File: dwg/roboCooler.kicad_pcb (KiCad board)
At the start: 2 copper layers, 100 x 81 mm, 54 parts, among them J1 CONN_01X02, J10 CONN_01X04, J11 CONN_01X04, J12 USB_A, J13 CONN_02X03, J14 CONN_02X03, J2 CONN_01X02, J3 Discovery_F407_P1, J4 CONN_01X06, J5 CONN_01X12, J6 Discovery_F407_P2, J7 CONN_02X03, J8 CONN_01X02, J9 CONN_01X02, Q1 NMOS, Q2 NMOS, SW1 SPST_4PIN, SW2 SPST_4PIN, U1 SN74LV, U2 TB6549

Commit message: moved led fan and pump to 6-pin conns
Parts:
- removed J9: CONN_01X02, Socket_Strips:Socket_Strip_Angled_1x02
- J10: value CONN_01X04 -> CONN_02X03; footprint Socket_Strips:Socket_Strip_Angled_1x04 -> Pin_Headers:Pin_Header_Angled_2x03
- J8: value CONN_01X02 -> CONN_02X03; footprint Socket_Strips:Socket_Strip_Angled_1x02 -> Pin_Headers:Pin_Header_Angled_2x03
- moved J10 10.2 mm to (54.7, 71.2), turned to 180 degrees
- moved J8 1.95 mm to (145.4, 97.2), turned to 0 degrees
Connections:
- J10 pad 4: GND -> Net-(J10-Pad4)
- J8 pad 2: Net-(D1-Pad2) -> +12V
- R7 pad 2: Net-(J10-Pad2) -> Net-(J10-Pad3)
- U1 pad 4: Net-(J10-Pad2) -> Net-(J10-Pad3)

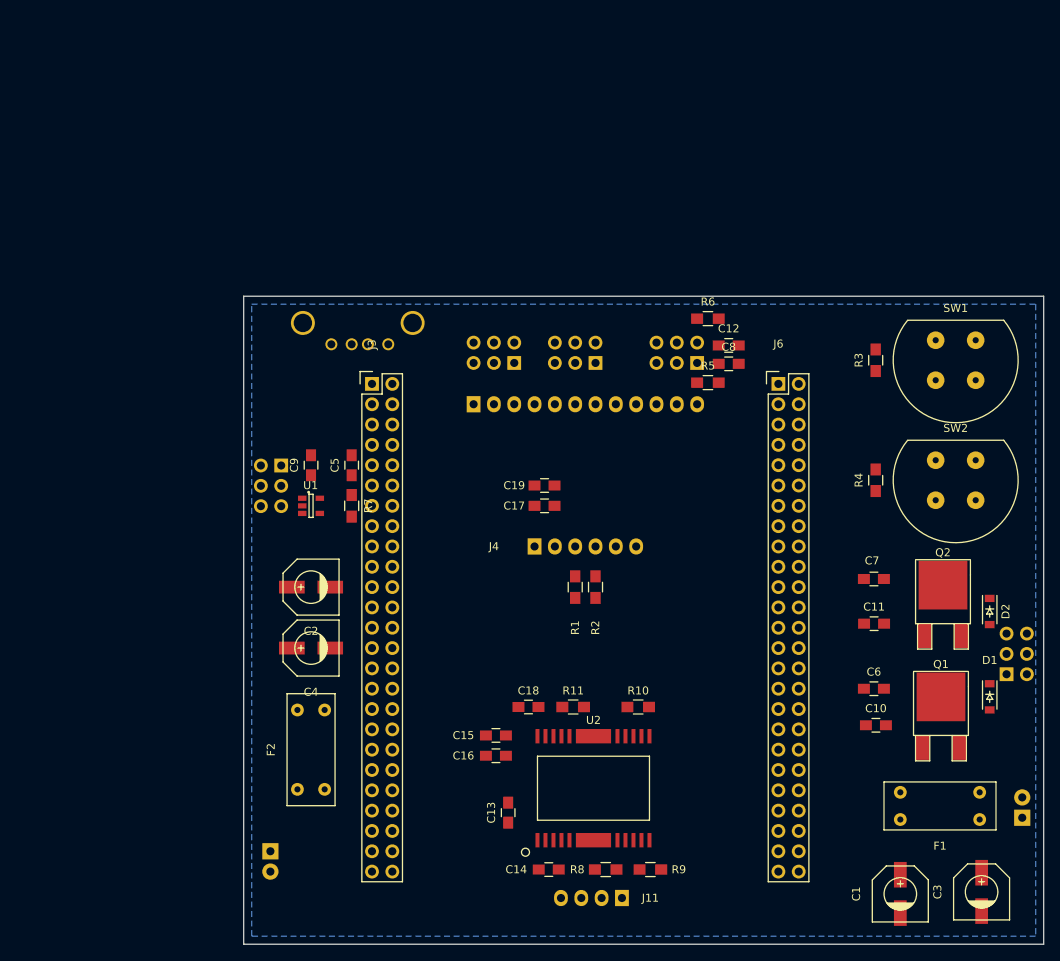
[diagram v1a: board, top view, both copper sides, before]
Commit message: moved all components inside the disc envelope
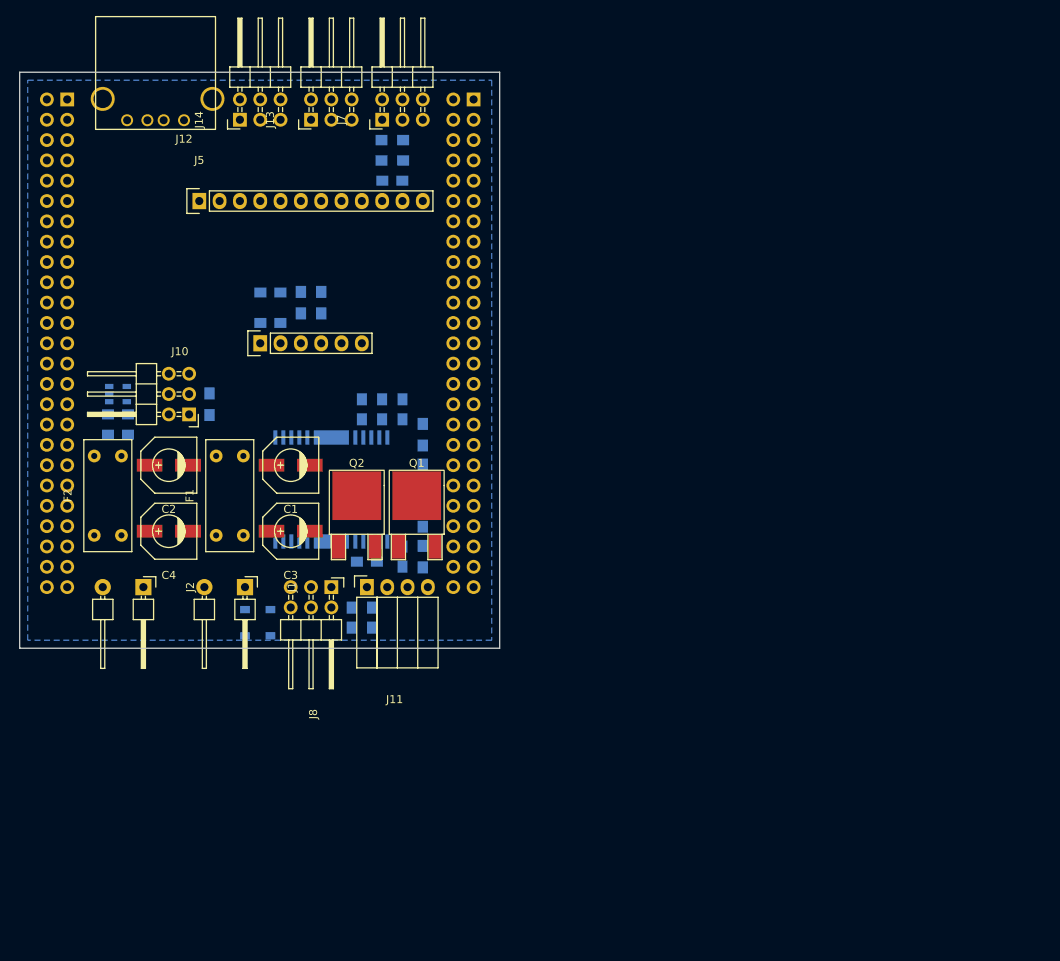
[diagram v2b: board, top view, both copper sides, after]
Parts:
- removed C11: 1UF, Capacitors_SMD:C_0805_HandSoldering
- removed C12: .1UF, Capacitors_SMD:C_0805_HandSoldering
- removed C7: .01UF, Capacitors_SMD:C_0805_HandSoldering
- removed R3, R4: 10k, Resistors_SMD:R_0805_HandSoldering
- removed SW1, SW2: SPST_4PIN, roboCooler:D6C90
- C10, C13, C14, C15, C16, C17, C18, C19, C5, C6, C8, C9, D1, D2, J3, J6, R1, R10, R11, R2, R5, R6, R7, R8, R9, U1, U2: moved to B.Cu
- J1, J2: footprint Pin_Headers:Pin_Header_Angled_1x02 -> roboCooler:Pin_Header_Angled_1x02_200mil; moved to F.Cu
- J10, J11, J12, J13, J14, J4, J5, J7, J8: moved to F.Cu
- moved J1 103.8 mm to (47.6, 86.4), turned to 270 degrees
- moved C3 97.4 mm to (55.9, 79.4), turned to 180 degrees
- moved F1 96.9 mm to (48.3, 74.9), turned to 90 degrees
- moved D1 93.6 mm to (50.2, 90.8), turned to 90 degrees
- moved C1 93.2 mm to (55.9, 71.1), turned to 180 degrees
- moved D2 89.9 mm to (53.3, 90.8), turned to 90 degrees
- moved J8 85.1 mm to (61.0, 86.4), turned to 270 degrees
- moved Q2 74.1 mm to (64.1, 81.3)
- moved Q1 70.2 mm to (71.6, 81.3)
- moved C6 65.9 mm to (63.5, 90.2), turned to 90 degrees
- moved C10 64.4 mm to (66.0, 90.2), turned to 90 degrees
- moved R8 59.0 mm to (72.4, 67.3), turned to 270 degrees
- moved R9 56.9 mm to (72.4, 72.4), turned to 90 degrees
- moved J3 55.9 mm to (25.4, 25.4)
- moved J6 55.9 mm to (76.2, 25.4)
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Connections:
- J3 pad 14: LED_UART -> Net-(J3-Pad14)
- J3 pad 40: Net-(J3-Pad40) -> LED_UART
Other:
- board size 100 x 81 mm -> 60 x 72 mm

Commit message: updated pcb design rules
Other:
- net class Default: clearance 0.2 -> 0.1524; trace_width 0.25 -> 0.1524; via_dia 0.6 -> 0.6858; via_drill 0.4 -> 0.3302
- rule trace_clearance: 0.2 -> 0.1524
- rule trace_min: 0.2 -> 0.1524
- rule via_min_drill: 0.3 -> 0.3302
- rule via_min_size: 0.4 -> 0.6858

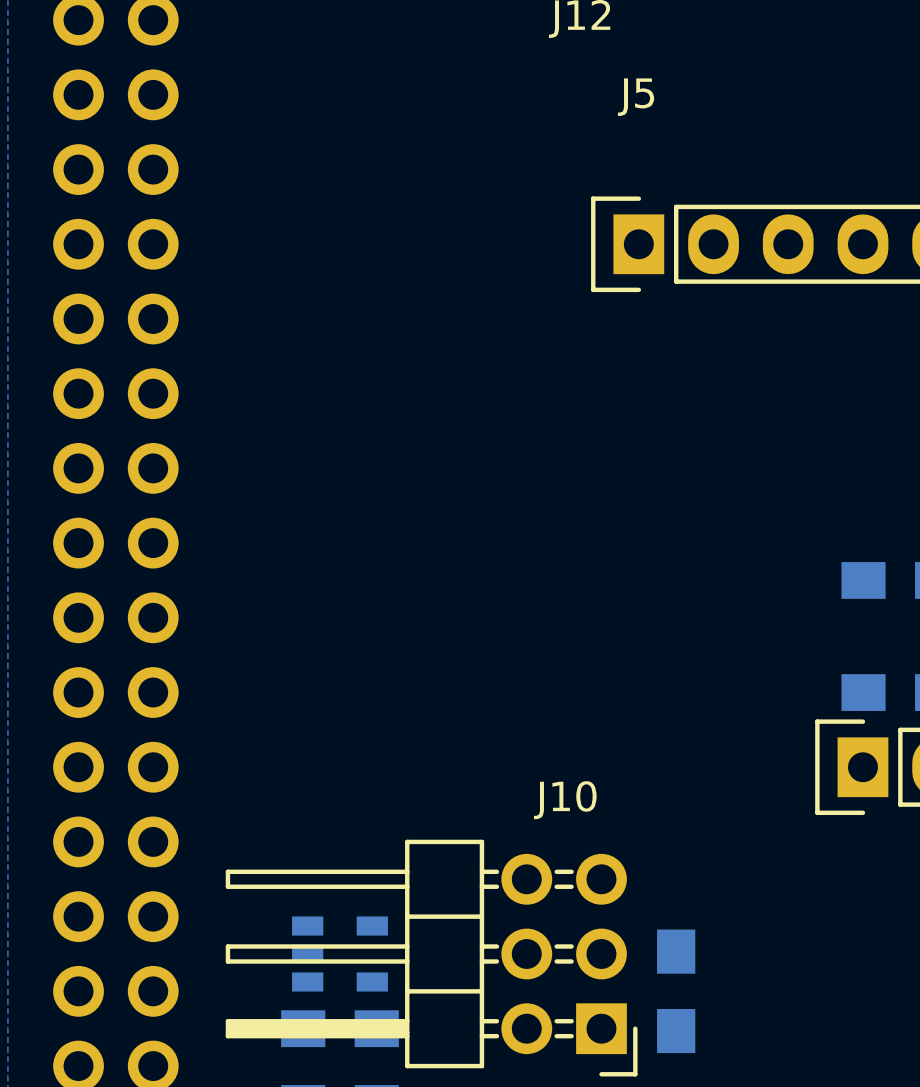
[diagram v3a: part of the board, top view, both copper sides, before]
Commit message: added 8 leds
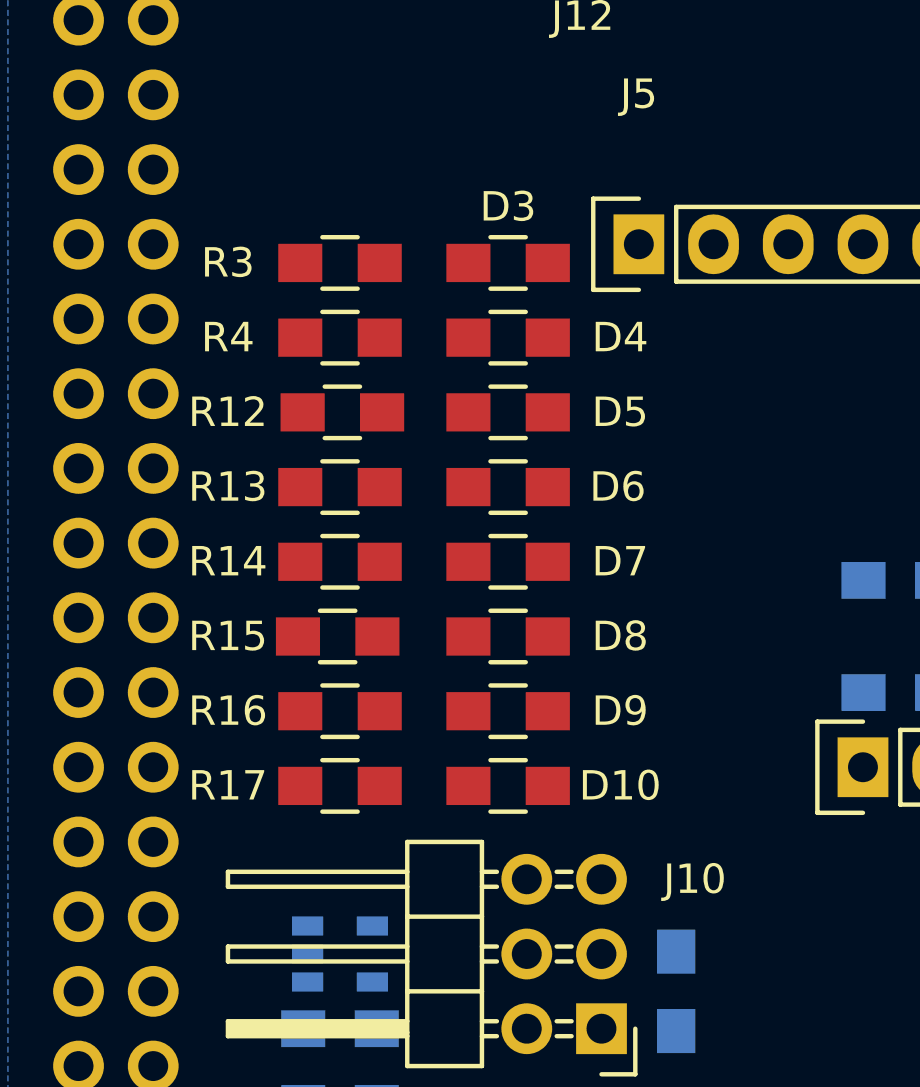
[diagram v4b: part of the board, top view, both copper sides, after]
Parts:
- added D10: Led_Small, Resistors_SMD:R_0805_HandSoldering, F.Cu at (40.0, 56.5)
- added D3: Led_Small, Resistors_SMD:R_0805_HandSoldering, F.Cu at (40.0, 38.7)
- added D4: Led_Small, Resistors_SMD:R_0805_HandSoldering, F.Cu at (40.0, 41.3)
- added D5: Led_Small, Resistors_SMD:R_0805_HandSoldering, F.Cu at (40.0, 43.8)
- added D6: Led_Small, Resistors_SMD:R_0805_HandSoldering, F.Cu at (40.0, 46.4)
- added D7: Led_Small, Resistors_SMD:R_0805_HandSoldering, F.Cu at (40.0, 48.9)
- added D8: Led_Small, Resistors_SMD:R_0805_HandSoldering, F.Cu at (40.0, 51.4)
- added D9: Led_Small, Resistors_SMD:R_0805_HandSoldering, F.Cu at (40.0, 54.0)
- added R12: 200, Resistors_SMD:R_0805_HandSoldering, F.Cu at (34.4, 43.8)
- added R13: 200, Resistors_SMD:R_0805_HandSoldering, F.Cu at (34.3, 46.4)
- added R14: 200, Resistors_SMD:R_0805_HandSoldering, F.Cu at (34.3, 48.9)
- added R15: 200, Resistors_SMD:R_0805_HandSoldering, F.Cu at (34.2, 51.4)
- added R16: 200, Resistors_SMD:R_0805_HandSoldering, F.Cu at (34.3, 54.0)
- added R17: 200, Resistors_SMD:R_0805_HandSoldering, F.Cu at (34.3, 56.5)
- added R3: 200, Resistors_SMD:R_0805_HandSoldering, F.Cu at (34.3, 38.7)
- added R4: 200, Resistors_SMD:R_0805_HandSoldering, F.Cu at (34.3, 41.3)
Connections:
- J3 pad 11: Net-(J3-Pad11) -> LED_1
- J3 pad 13: Net-(J3-Pad13) -> LED_2
- J3 pad 17: Net-(J3-Pad17) -> LED_3
- J3 pad 19: Net-(J3-Pad19) -> LED_4
- J3 pad 21: Net-(J3-Pad21) -> LED_5
- J3 pad 25: Net-(J3-Pad25) -> LED_6
- J3 pad 27: Net-(J3-Pad27) -> LED_7
- J3 pad 7: Net-(J3-Pad7) -> LED_0

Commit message: first pass at layout
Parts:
- moved Q1 7.49 mm to (64.1, 81.3)
- moved Q2 7.49 mm to (71.6, 81.3)
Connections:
- J13 pad 1: CS_0 -> CS_5
- J13 pad 2: CS_3 -> CS_4
- J13 pad 3: CS_1 -> CS_3
- J13 pad 4: CS_4 -> CS_2
- J13 pad 5: CS_2 -> CS_1
- J13 pad 6: CS_5 -> CS_0
- J14 pad 1: CS_6 -> CS_11
- J14 pad 2: CS_9 -> CS_10
- J14 pad 3: CS_7 -> CS_9
- J14 pad 4: CS_10 -> CS_8
- J14 pad 5: CS_8 -> CS_7
- J14 pad 6: CS_11 -> CS_6
- J6 pad 22: VDD -> VEE
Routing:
- net +5V: track 0.00 -> 75.1 mm
- net +12V: track 0.00 -> 71.7 mm, vias 0 -> 2
- net +3V3: track 0.00 -> 57.0 mm, vias 0 -> 1
- net GND: track 0.00 -> 52.3 mm, vias 0 -> 10
- net CS_IRQ: track 0.00 -> 31.5 mm
- net MOTOR_IN1: track 0.00 -> 27.7 mm, vias 0 -> 2
- net CS_SCL: track 0.00 -> 27.5 mm, vias 0 -> 1
- net MOTOR_IN2: track 0.00 -> 26.8 mm, vias 0 -> 2
- net MOTOR_PWM: track 0.00 -> 26.8 mm
- net MOTOR_OUT2: track 0.00 -> 25.6 mm
- net MOTOR_SB: track 0.00 -> 24.9 mm, vias 0 -> 2
- net FAN: track 0.00 -> 22.2 mm
- net HALL_2: track 0.00 -> 20.9 mm
- net CS_SDA: track 0.00 -> 20.8 mm, vias 0 -> 1
- net Net-(D2-Pad2): track 0.00 -> 20.6 mm
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
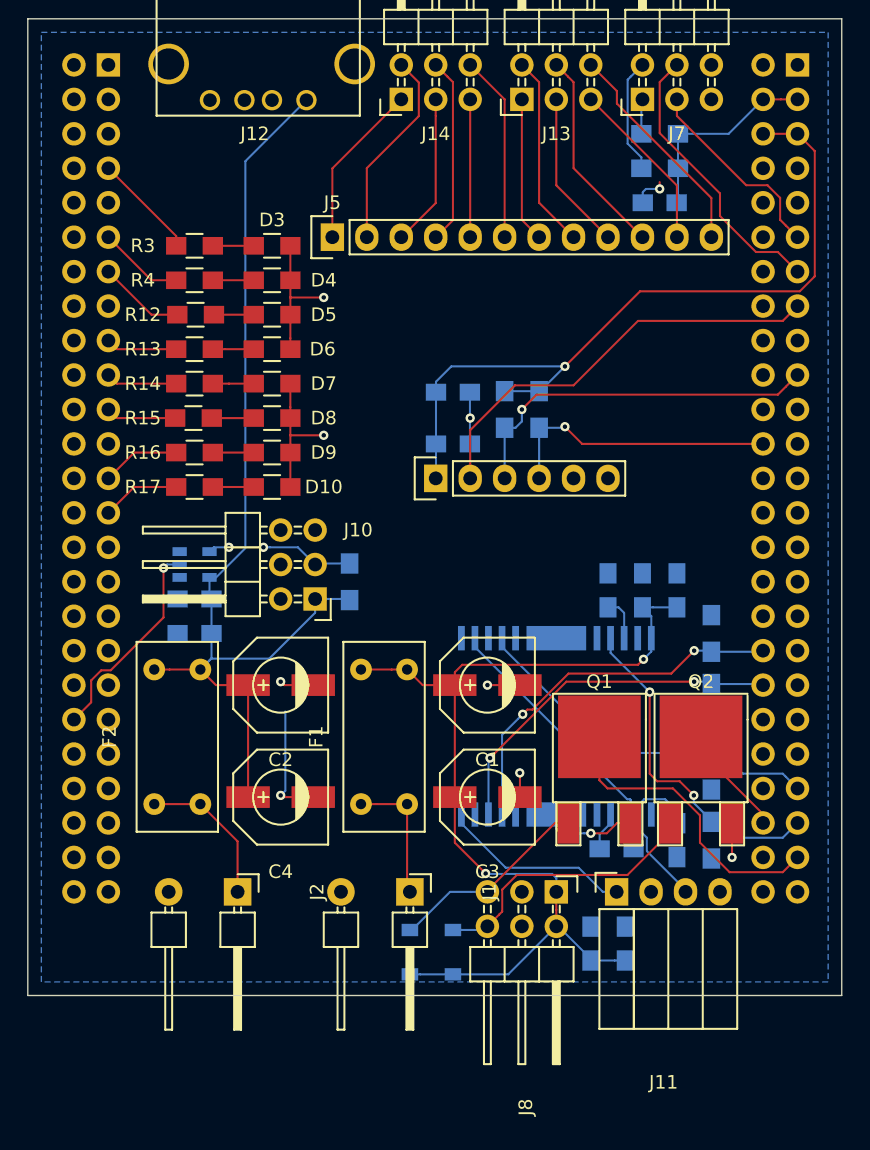
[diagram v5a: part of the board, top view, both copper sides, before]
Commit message: increased size of pcb power nets and reordered some components.
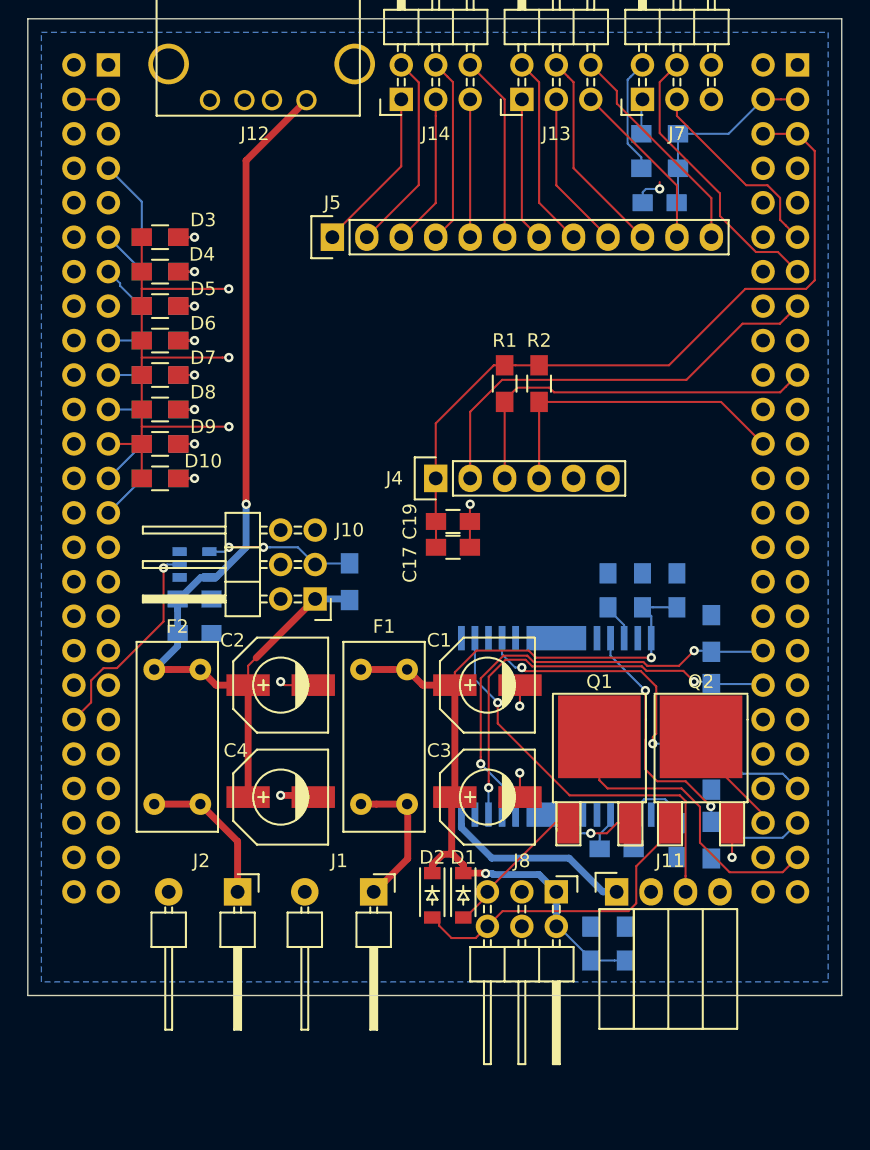
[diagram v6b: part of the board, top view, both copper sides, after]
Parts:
- C17, C19, D1, D2, R1, R2: moved to F.Cu
- R12, R13, R14, R15, R16, R17, R3, R4: moved to B.Cu
- moved C19 9.52 mm to (53.3, 59.1)
- moved D10 8.28 mm to (31.8, 55.9), turned to 0 degrees
- moved D3 8.28 mm to (31.8, 38.1), turned to 0 degrees
- moved D4 8.28 mm to (31.8, 40.6), turned to 0 degrees
- moved D5 8.28 mm to (31.8, 43.2), turned to 0 degrees
- moved D6 8.28 mm to (31.8, 45.7), turned to 0 degrees
- moved D7 8.28 mm to (31.8, 48.3), turned to 0 degrees
- moved D8 8.28 mm to (31.8, 50.8), turned to 0 degrees
- moved D9 8.28 mm to (31.8, 53.3), turned to 0 degrees
- moved C17 7.62 mm to (53.3, 61.0)
- moved D1 5.75 mm to (54.1, 86.6), turned to 270 degrees
- moved D2 4.46 mm to (51.8, 86.6), turned to 270 degrees
- moved R12 2.70 mm to (31.8, 43.2)
- moved J1 2.67 mm to (45.0, 86.4)
- moved R14 2.62 mm to (31.8, 48.3)
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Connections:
- J10 pad 2: Net-(J10-Pad2) -> (no net)
- J10 pad 4: Net-(J10-Pad4) -> (no net)
- J10 pad 6: Net-(J10-Pad6) -> (no net)
- J12 pad 2: Net-(J12-Pad2) -> (no net)
- J12 pad 3: Net-(J12-Pad3) -> (no net)
- J3 pad 10: Net-(J3-Pad10) -> (no net)
- J3 pad 12: Net-(J3-Pad12) -> (no net)
- J3 pad 14: Net-(J3-Pad14) -> (no net)
- J3 pad 15: Net-(J3-Pad15) -> (no net)
- J3 pad 16: Net-(J3-Pad16) -> (no net)
- J3 pad 18: Net-(J3-Pad18) -> (no net)
- J3 pad 20: Net-(J3-Pad20) -> (no net)
- J3 pad 22: Net-(J3-Pad22) -> (no net)
- J3 pad 24: Net-(J3-Pad24) -> (no net)
- J3 pad 26: Net-(J3-Pad26) -> (no net)
- J3 pad 28: Net-(J3-Pad28) -> (no net)
- J3 pad 29: Net-(J3-Pad29) -> (no net)
- J3 pad 30: Net-(J3-Pad30) -> (no net)
- J3 pad 31: Net-(J3-Pad31) -> (no net)
- J3 pad 32: Net-(J3-Pad32) -> (no net)
- J3 pad 33: Net-(J3-Pad33) -> (no net)
- J3 pad 34: Net-(J3-Pad34) -> (no net)
- J3 pad 35: Net-(J3-Pad35) -> (no net)
- J3 pad 36: Net-(J3-Pad36) -> (no net)
- J3 pad 37: Net-(J3-Pad37) -> (no net)
- J3 pad 38: Net-(J3-Pad38) -> (no net)
- J3 pad 39: Net-(J3-Pad39) -> (no net)
- J3 pad 41: Net-(J3-Pad41) -> (no net)
- J3 pad 42: Net-(J3-Pad42) -> (no net)
- J3 pad 43: Net-(J3-Pad43) -> (no net)
- J3 pad 44: Net-(J3-Pad44) -> (no net)
- J3 pad 45: Net-(J3-Pad45) -> (no net)
- J3 pad 46: Net-(J3-Pad46) -> (no net)
- J3 pad 47: Net-(J3-Pad47) -> (no net)
- J3 pad 48: Net-(J3-Pad48) -> (no net)
- J3 pad 6: Net-(J3-Pad6) -> (no net)
- J3 pad 8: Net-(J3-Pad8) -> (no net)
- J3 pad 9: Net-(J3-Pad9) -> (no net)
- J4 pad 5: Net-(J4-Pad5) -> (no net)
- J6 pad 10: Net-(J6-Pad10) -> (no net)
- J6 pad 12: PUSH_UP -> (no net)
- J6 pad 14: PUSH_DN -> (no net)
- J6 pad 16: Net-(J6-Pad16) -> (no net)
- J6 pad 17: Net-(J6-Pad17) -> (no net)
- J6 pad 18: Net-(J6-Pad18) -> (no net)
- J6 pad 20: Net-(J6-Pad20) -> (no net)
- J6 pad 21: Net-(J6-Pad21) -> (no net)
- J6 pad 22: VEE -> (no net)
- J6 pad 23: Net-(J6-Pad23) -> (no net)
- J6 pad 25: Net-(J6-Pad25) -> (no net)
- J6 pad 26: Net-(J6-Pad26) -> (no net)
- J6 pad 27: Net-(J6-Pad27) -> (no net)
- J6 pad 28: Net-(J6-Pad28) -> (no net)
- J6 pad 29: Net-(J6-Pad29) -> (no net)
- J6 pad 30: Net-(J6-Pad30) -> (no net)
- J6 pad 31: Net-(J6-Pad31) -> (no net)
- J6 pad 32: Net-(J6-Pad32) -> (no net)
- J6 pad 33: Net-(J6-Pad33) -> (no net)
- J6 pad 34: Net-(J6-Pad34) -> (no net)
- J6 pad 35: Net-(J6-Pad35) -> (no net)
- J6 pad 37: Net-(J6-Pad37) -> (no net)
- J6 pad 39: Net-(J6-Pad39) -> (no net)
- J6 pad 40: Net-(J6-Pad40) -> (no net)
- J6 pad 41: Net-(J6-Pad41) -> (no net)
- J6 pad 42: Net-(J6-Pad42) -> (no net)
- J6 pad 44: Net-(J6-Pad44) -> (no net)
- J6 pad 48: Net-(J6-Pad48) -> (no net)
- J6 pad 7: Net-(J6-Pad7) -> (no net)
- J6 pad 8: Net-(J6-Pad8) -> (no net)
- J6 pad 9: Net-(J6-Pad9) -> (no net)
- J8 pad 3: Net-(J8-Pad3) -> (no net)
- J8 pad 4: Net-(J8-Pad4) -> (no net)
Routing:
- net GND: track 52.3 -> 64.1 mm, vias 10 -> 11
- net +12V: track 71.7 -> 63.3 mm
- net MOTOR_IN1: track 27.7 -> 33.0 mm
- net MOTOR_IN2: track 26.8 -> 31.7 mm
- net MOTOR_OUT2: track 25.6 -> 30.0 mm, vias 0 -> 1
- net Net-(D1-Pad2): track 15.0 -> 10.8 mm
- net Net-(D2-Pad2): track 20.6 -> 23.9 mm
- net MOTOR_PWM: track 26.8 -> 29.9 mm, vias 0 -> 2
- net LED_4: track 5.26 -> 2.46 mm
- net LED_3: track 5.26 -> 2.46 mm
- net LED_2: track 6.40 -> 3.62 mm
- net LED_1: track 6.32 -> 3.56 mm
- net LED_5: track 5.18 -> 2.46 mm
- net CS_SDA: track 20.8 -> 23.4 mm, vias 1 -> 0
- net VDD: track 0.00 -> 2.54 mm
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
